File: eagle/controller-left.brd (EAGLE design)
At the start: 75 x 50 mm, 7 parts, among them U1 JOYSTICKPTH

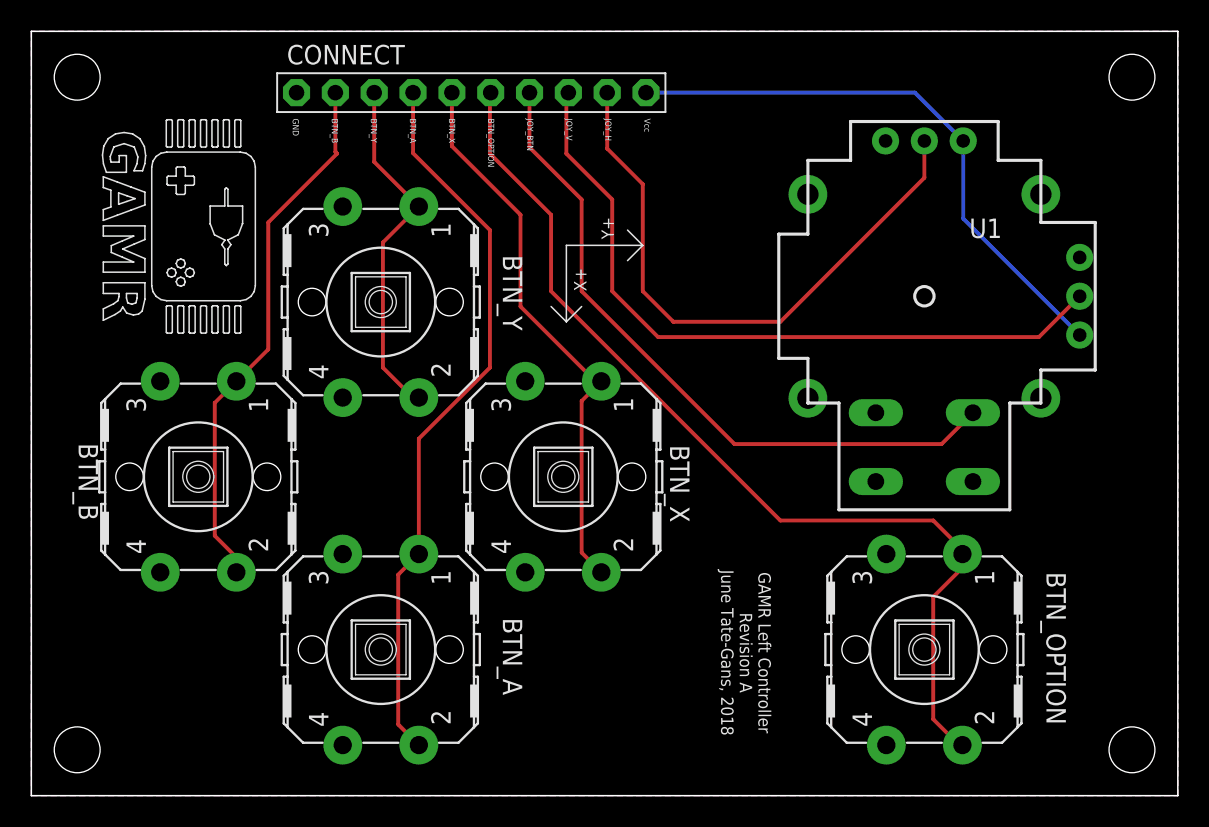
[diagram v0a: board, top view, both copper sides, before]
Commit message: left-controller: Fix some silkscreen issues.
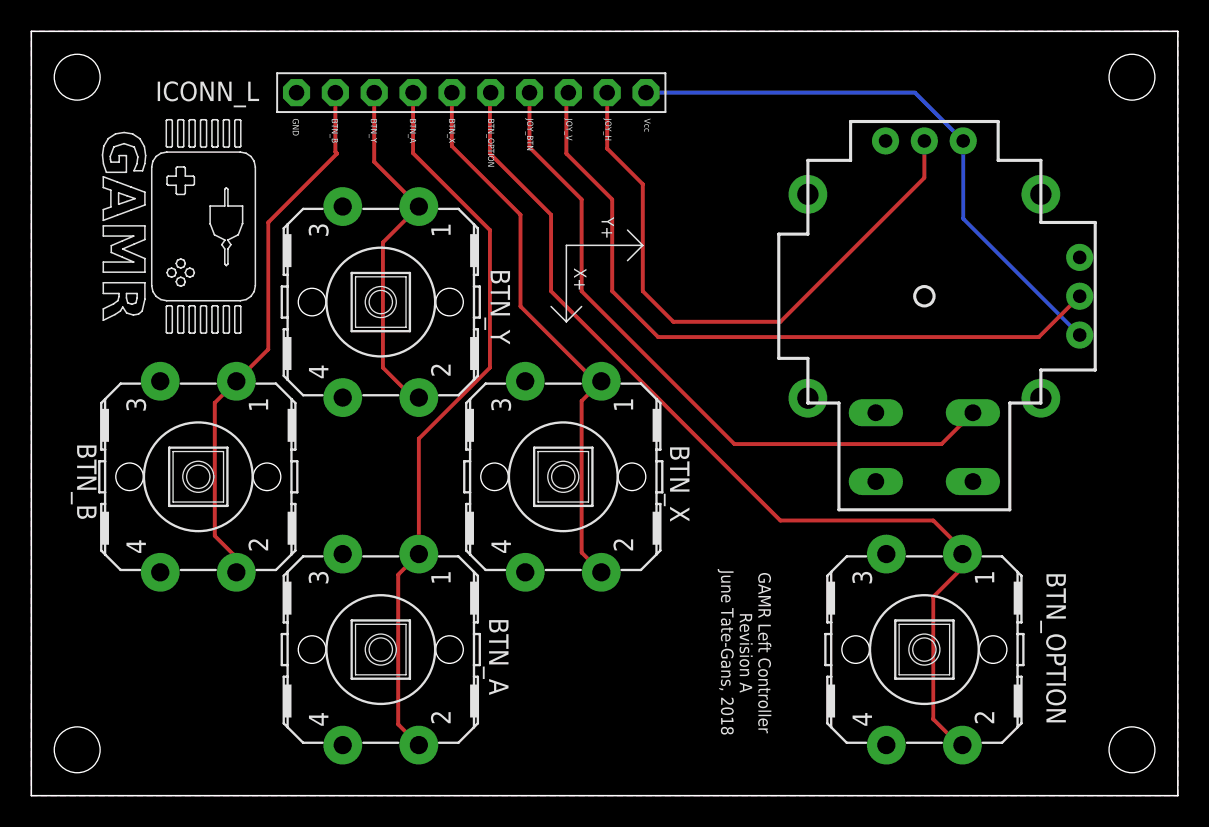
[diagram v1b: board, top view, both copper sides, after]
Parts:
- renumbered CONNECT to ICONN_L, U1 to JOYSTICK
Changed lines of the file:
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@@
 <wire x1="35" y1="31" x2="36" y2="32" width="0.1" layer="21"/>
 <wire x1="34" y1="32" x2="35" y2="31" width="0.1" layer="21"/>
-<text x="35.5" y="33" size="0.8128" layer="21" font="vector" rot="R270" align="bottom-right">X+</text>
-<text x="37.3" y="36.4" size="0.8128" layer="21" font="vector" rot="R270" align="bottom-right">Y+</text>
+<text x="35.5" y="33" size="0.8128" layer="21" font="vector" rot="SR270" align="bottom-right">X+</text>
+<text x="37.3" y="36.4" size="0.8128" layer="21" font="vector" rot="SR270" align="bottom-right">Y+</text>
 <hole x="3" y="3" drill="3"/>
 <hole x="3" y="47" drill="3"/>
@@
 </autorouter>
 <elements>
-<element name="U1" library="adafruit" package="JOYSTICK" value="JOYSTICKPTH" x="58.42" y="32.671" rot="R180"/>
+<element name="JOYSTICK" library="adafruit" package="JOYSTICK" value="JOYSTICKPTH" x="58.42" y="32.671" smashed="yes" rot="R180">
+<attribute name="VALUE" x="63.5" y="39.021" size="1.27" layer="27" rot="R180"/>
+</element>
 <element name="BTN_A" library="adafruit" package="B3F-40XX-ROUND" value="" x="22.86" y="9.557" smashed="yes" rot="R270">
-<attribute name="NAME" x="30.845" y="11.637" size="1.27" layer="25" ratio="10" rot="SR270"/>
+<attribute name="NAME" x="29.945" y="11.637" size="1.27" layer="25" ratio="10" rot="SR270"/>
 <attribute name="VALUE" x="17.78" y="12.732" size="1.27" layer="27" ratio="10" rot="R270"/>
 </element>
 <element name="BTN_B" library="adafruit" package="B3F-40XX-ROUND" value="" x="10.922" y="20.86" smashed="yes" rot="R270">
-<attribute name="NAME" x="3.093" y="23.06" size="1.27" layer="25" ratio="10" rot="SR270"/>
+<attribute name="NAME" x="2.993" y="23.06" size="1.27" layer="25" ratio="10" rot="SR270"/>
 <attribute name="VALUE" x="5.842" y="24.035" size="1.27" layer="27" ratio="10" rot="R270"/>
 </element>
@@
 </element>
 <element name="BTN_Y" library="adafruit" package="B3F-40XX-ROUND" value="" x="22.86" y="32.29" smashed="yes" rot="R270">
-<attribute name="NAME" x="30.845" y="35.37" size="1.27" layer="25" ratio="10" rot="SR270"/>
+<attribute name="NAME" x="30.045" y="34.47" size="1.27" layer="25" ratio="10" rot="SR270"/>
 <attribute name="VALUE" x="17.78" y="35.465" size="1.27" layer="27" ratio="10" rot="R270"/>
 </element>
@@
 <attribute name="VALUE" x="53.34" y="12.732" size="1.27" layer="27" ratio="10" rot="R270"/>
 </element>
-<element name="CONNECT" library="adafruit" package="1X10-BIG" value="PINHD-1X10" x="28.78" y="45.99" smashed="yes" rot="R180">
-<attribute name="NAME" x="16.7138" y="47.8388" size="1.27" layer="25" ratio="10"/>
+<element name="ICONN_L" library="adafruit" package="1X10-BIG" value="PINHD-1X10" x="28.78" y="45.99" smashed="yes" rot="R180">
+<attribute name="NAME" x="8.1138" y="45.4388" size="1.27" layer="25" ratio="10"/>
 <attribute name="VALUE" x="40.21" y="49.165" size="1.27" layer="27" rot="R180"/>
 </element>
@@
 <contactref element="BTN_OPTION" pad="3"/>
 <contactref element="BTN_OPTION" pad="4"/>
-<contactref element="U1" pad="V3"/>
-<contactref element="U1" pad="H3"/>
-<contactref element="CONNECT" pad="10"/>
+<contactref element="JOYSTICK" pad="V3"/>
+<contactref element="JOYSTICK" pad="H3"/>
+<contactref element="ICONN_L" pad="10"/>
 <polygon width="0.1" layer="1" isolate="0.012">
 <vertex x="0" y="50"/>
@@
 <vertex x="75" y="50"/>
 </polygon>
-<contactref element="U1" pad="B1A"/>
+<contactref element="JOYSTICK" pad="B1A"/>
 </signal>
 <signal name="BTN_A">
 <contactref element="BTN_A" pad="1"/>
 <contactref element="BTN_A" pad="2"/>
-<contactref element="CONNECT" pad="7"/>
+<contactref element="ICONN_L" pad="7"/>
 <wire x1="25.3492" y1="15.8054" x2="25.3492" y2="23.3492" width="0.254" layer="1"/>
 <wire x1="25.3492" y1="23.3492" x2="30" y2="28" width="0.254" layer="1"/>
@@
 <contactref element="BTN_B" pad="1"/>
 <contactref element="BTN_B" pad="2"/>
-<contactref element="CONNECT" pad="9"/>
+<contactref element="ICONN_L" pad="9"/>
 <wire x1="13.4112" y1="27.1084" x2="12" y2="25.6972" width="0.254" layer="1"/>
 <wire x1="12" y1="17" x2="13.4112" y2="15.5888" width="0.254" layer="1"/>
@@
 <contactref element="BTN_X" pad="2"/>
 <wire x1="37.2872" y1="27.1084" x2="37.2872" y2="27" width="0.254" layer="1"/>
-<contactref element="CONNECT" pad="6"/>
+<contactref element="ICONN_L" pad="6"/>
 <wire x1="27.51" y1="45.99" x2="27.51" y2="42.49" width="0.254" layer="1"/>
 <wire x1="32" y1="38" x2="32" y2="32" width="0.254" layer="1"/>
@@
 <contactref element="BTN_Y" pad="1"/>
 <contactref element="BTN_Y" pad="2"/>
-<contactref element="CONNECT" pad="8"/>
+<contactref element="ICONN_L" pad="8"/>
 <wire x1="25.3492" y1="38.5384" x2="22.43" y2="41.4576" width="0.254" layer="1"/>
 <wire x1="22.43" y1="41.4576" x2="22.43" y2="45.99" width="0.254" layer="1"/>
@@
 <contactref element="BTN_OPTION" pad="1"/>
 <contactref element="BTN_OPTION" pad="2"/>
-<contactref element="CONNECT" pad="5"/>
+<contactref element="ICONN_L" pad="5"/>
 <wire x1="30.05" y1="45.99" x2="30" y2="45.94" width="0.254" layer="1"/>
 <wire x1="30" y1="45.94" x2="30" y2="42" width="0.254" layer="1"/>
@@
 </signal>
 <signal name="VCC">
-<contactref element="U1" pad="V1"/>
-<contactref element="U1" pad="H1"/>
-<contactref element="CONNECT" pad="1"/>
+<contactref element="JOYSTICK" pad="V1"/>
+<contactref element="JOYSTICK" pad="H1"/>
+<contactref element="ICONN_L" pad="1"/>
 <wire x1="40.21" y1="45.99" x2="57.801" y2="45.99" width="0.254" layer="16"/>
 <wire x1="57.801" y1="45.99" x2="60.96" y2="42.831" width="0.254" layer="16"/>
@@
 </signal>
 <signal name="JOY_V">
-<contactref element="U1" pad="V2"/>
-<contactref element="CONNECT" pad="3"/>
+<contactref element="JOYSTICK" pad="V2"/>
+<contactref element="ICONN_L" pad="3"/>
 <wire x1="68.58" y1="32.671" x2="65.909" y2="30" width="0.254" layer="1"/>
 <wire x1="65.909" y1="30" x2="41" y2="30" width="0.254" layer="1"/>
@@
 </signal>
 <signal name="JOY_H">
-<contactref element="U1" pad="H2"/>
-<contactref element="CONNECT" pad="2"/>
+<contactref element="JOYSTICK" pad="H2"/>
+<contactref element="ICONN_L" pad="2"/>
 <wire x1="58.42" y1="42.831" x2="58.42" y2="40.42" width="0.254" layer="1"/>
 <wire x1="49" y1="31" x2="42" y2="31" width="0.254" layer="1"/>
@@
 </signal>
 <signal name="JOY_BTN">
-<contactref element="U1" pad="B2A"/>
-<contactref element="CONNECT" pad="4"/>
+<contactref element="JOYSTICK" pad="B2A"/>
+<contactref element="ICONN_L" pad="4"/>
 <wire x1="61.595" y1="25.051" x2="59.544" y2="23" width="0.254" layer="1"/>
 <wire x1="59.544" y1="23" x2="46" y2="23" width="0.254" layer="1"/>

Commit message: left-controller: Routing adjustments
The previews for the routing of lines inside the omron tactile switches
was a bit too tight for the copper pour. Moved them away from some of
the pads to compensate.

Also minor silkscreen touches to indicate pin 1 on the ICONN_L header.
Should prevent misorientation of the interconnects.
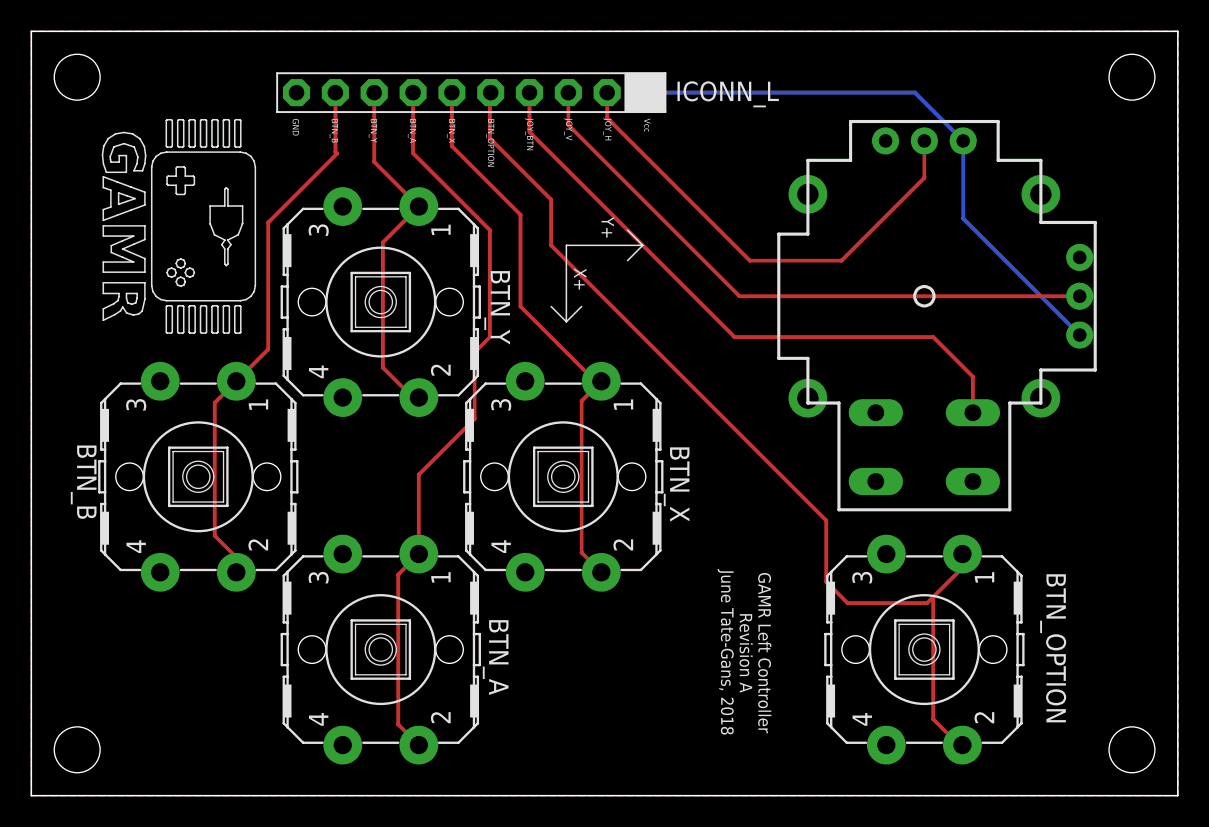
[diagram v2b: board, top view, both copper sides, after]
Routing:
- net JOY_H: track 39.5 -> 30.9 mm
- net JOY_V: track 47.2 -> 40.2 mm
- net JOY_BTN: track 45.0 -> 40.6 mm
